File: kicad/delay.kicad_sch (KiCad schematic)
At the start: 58 parts, among them Q1 2N3904, U3 TL074, U4 TL072, U5 PT2399, U6 4020

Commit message: component positioning mostly done
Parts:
- C10, C11, C12, C16, C17, C19, C29, C30, C8: footprint rumblesan-standard-parts:C_Rect_L7.0mm_W3.5mm_P5.00mm -> rumblesan-standard-parts:C_Rect_L7.0mm_W2.5mm_P5.00mm
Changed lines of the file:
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@@
       (effects (font (size 1.27 1.27)) (justify left))
     )
-    (property "Footprint" "rumblesan-standard-parts:C_Rect_L7.0mm_W3.5mm_P5.00mm" (id 2) (at 114.935 232.41 90)
+    (property "Footprint" "rumblesan-standard-parts:C_Rect_L7.0mm_W2.5mm_P5.00mm" (id 2) (at 114.935 232.41 90)
       (effects (font (size 1.27 1.27)) hide)
     )
@@
       (effects (font (size 1.27 1.27)) (justify left))
     )
-    (property "Footprint" "rumblesan-standard-parts:C_Rect_L7.0mm_W3.5mm_P5.00mm" (id 2) (at 114.935 219.71 90)
+    (property "Footprint" "rumblesan-standard-parts:C_Rect_L7.0mm_W2.5mm_P5.00mm" (id 2) (at 114.935 219.71 90)
       (effects (font (size 1.27 1.27)) hide)
     )
@@
       (effects (font (size 1.27 1.27)) (justify left))
     )
-    (property "Footprint" "rumblesan-standard-parts:C_Rect_L7.0mm_W3.5mm_P5.00mm" (id 2) (at 86.995 232.41 90)
+    (property "Footprint" "rumblesan-standard-parts:C_Rect_L7.0mm_W2.5mm_P5.00mm" (id 2) (at 86.995 232.41 90)
       (effects (font (size 1.27 1.27)) hide)
     )
@@
     (property "Reference" "C29" (id 0) (at 288.29 22.8092 90))
     (property "Value" "10pF" (id 1) (at 288.29 25.1206 90))
-    (property "Footprint" "rumblesan-standard-parts:C_Rect_L7.0mm_W3.5mm_P5.00mm" (id 2) (at 289.56 34.925 0)
+    (property "Footprint" "rumblesan-standard-parts:C_Rect_L7.0mm_W2.5mm_P5.00mm" (id 2) (at 289.56 34.925 0)
       (effects (font (size 1.27 1.27)) hide)
     )
@@
     (property "Reference" "C19" (id 0) (at 121.92 48.2092 90))
     (property "Value" "10pF" (id 1) (at 121.92 50.5206 90))
-    (property "Footprint" "rumblesan-standard-parts:C_Rect_L7.0mm_W3.5mm_P5.00mm" (id 2) (at 123.19 60.325 0)
+    (property "Footprint" "rumblesan-standard-parts:C_Rect_L7.0mm_W2.5mm_P5.00mm" (id 2) (at 123.19 60.325 0)
       (effects (font (size 1.27 1.27)) hide)
     )
@@
     (property "Reference" "C8" (id 0) (at 62.23 24.0792 90))
     (property "Value" "10pF" (id 1) (at 62.23 26.3906 90))
-    (property "Footprint" "rumblesan-standard-parts:C_Rect_L7.0mm_W3.5mm_P5.00mm" (id 2) (at 63.5 36.195 0)
+    (property "Footprint" "rumblesan-standard-parts:C_Rect_L7.0mm_W2.5mm_P5.00mm" (id 2) (at 63.5 36.195 0)
       (effects (font (size 1.27 1.27)) hide)
     )
@@
     (property "Reference" "C30" (id 0) (at 340.36 43.1292 90))
     (property "Value" "10pF" (id 1) (at 340.36 45.4406 90))
-    (property "Footprint" "rumblesan-standard-parts:C_Rect_L7.0mm_W3.5mm_P5.00mm" (id 2) (at 341.63 55.245 0)
+    (property "Footprint" "rumblesan-standard-parts:C_Rect_L7.0mm_W2.5mm_P5.00mm" (id 2) (at 341.63 55.245 0)
       (effects (font (size 1.27 1.27)) hide)
     )
@@
       (effects (font (size 1.27 1.27)) (justify left))
     )
-    (property "Footprint" "rumblesan-standard-parts:C_Rect_L7.0mm_W3.5mm_P5.00mm" (id 2) (at 86.995 219.71 90)
+    (property "Footprint" "rumblesan-standard-parts:C_Rect_L7.0mm_W2.5mm_P5.00mm" (id 2) (at 86.995 219.71 90)
       (effects (font (size 1.27 1.27)) hide)
     )
@@
       (effects (font (size 1.27 1.27)) (justify right))
     )
-    (property "Footprint" "rumblesan-standard-parts:C_Rect_L7.0mm_W3.5mm_P5.00mm" (id 2) (at 70.485 140.97 0)
-      (effects (font (size 1.27 1.27)) hide)
-    )
+    (property "Footprint" "rumblesan-standard-parts:C_Rect_L7.0mm_W2.5mm_P5.00mm" (id 2) (at 70.485 140.97 0)
+      (effects (font (size 1.27 1.27)) hide)
+    )

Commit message: initial layout done
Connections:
- net DRY_AUDIO_SOURCE: now also U3.14; no longer U3.7
- net FEEDBACK_SOURCE: now also U3.1; no longer U3.8
- net at C8.2, D5.2 (A), D6.1 (K)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: now also U3.13 (-); no longer U3.6 (-)
- net at C19.1, C22.1, R15.2: now also U3.8; no longer U3.1
- net at C19.2, R13.2, R14.2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: now also U3.9 (-); no longer U3.2 (-)
- net at C29.2, D10.2 (A), D11.1 (K)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: now also U3.2 (-); no longer U3.9 (-)
- net at C30.1, R29.2, R30.1: now also U3.7; no longer U3.14
- net at C30.2, R27.2, R28.1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: now also U3.6 (-); no longer U3.13 (-)
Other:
- moved on the sheet: U3A, U3B, U3C, U3D
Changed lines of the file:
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@@
     (pin "2")
   )
-  (symbol (lib_id "Amplifier_Operational:TL074") (at 62.23 76.2 0) (mirror x) (unit 2)
-    (in_bom yes) (on_board yes) (fields_autoplaced)
-    (property "Reference" "U3" (id 0) (at 62.23 67.4202 0))
-    (property "Value" "TL074" (id 1) (at 62.23 69.9571 0))
-    (property "Footprint" "rumblesan-standard-parts:DIP-14_W7.62mm_Socket" (id 2) (at 60.96 78.74 0)
-      (effects (font (size 1.27 1.27)) hide)
-    )
-    (property "Datasheet" "http://www.ti.com/lit/ds/symlink/tl071.pdf" (id 3) (at 63.5 81.28 0)
+  (symbol (lib_id "Amplifier_Operational:TL074") (at 340.36 74.93 0) (mirror x) (unit 2)
+    (in_bom yes) (on_board yes) (fields_autoplaced)
+    (property "Reference" "U3" (id 0) (at 340.36 66.1502 0))
+    (property "Value" "TL074" (id 1) (at 340.36 68.6871 0))
+    (property "Footprint" "rumblesan-standard-parts:DIP-14_W7.62mm_Socket" (id 2) (at 339.09 77.47 0)
+      (effects (font (size 1.27 1.27)) hide)
+    )
+    (property "Datasheet" "http://www.ti.com/lit/ds/symlink/tl071.pdf" (id 3) (at 341.63 80.01 0)
       (effects (font (size 1.27 1.27)) hide)
     )
@@
     (pin "2")
   )
-  (symbol (lib_id "Amplifier_Operational:TL074") (at 121.92 78.74 0) (mirror x) (unit 1)
-    (in_bom yes) (on_board yes) (fields_autoplaced)
-    (property "Reference" "U3" (id 0) (at 121.92 69.9602 0))
-    (property "Value" "TL074" (id 1) (at 121.92 72.4971 0))
-    (property "Footprint" "rumblesan-standard-parts:DIP-14_W7.62mm_Socket" (id 2) (at 120.65 81.28 0)
-      (effects (font (size 1.27 1.27)) hide)
-    )
-    (property "Datasheet" "http://www.ti.com/lit/ds/symlink/tl071.pdf" (id 3) (at 123.19 83.82 0)
+  (symbol (lib_id "Amplifier_Operational:TL074") (at 288.29 72.39 0) (mirror x) (unit 1)
+    (in_bom yes) (on_board yes) (fields_autoplaced)
+    (property "Reference" "U3" (id 0) (at 288.29 63.6102 0))
+    (property "Value" "TL074" (id 1) (at 288.29 66.1471 0))
+    (property "Footprint" "rumblesan-standard-parts:DIP-14_W7.62mm_Socket" (id 2) (at 287.02 74.93 0)
+      (effects (font (size 1.27 1.27)) hide)
+    )
+    (property "Datasheet" "http://www.ti.com/lit/ds/symlink/tl071.pdf" (id 3) (at 289.56 77.47 0)
       (effects (font (size 1.27 1.27)) hide)
     )
@@
     (pin "2")
   )
-  (symbol (lib_id "Amplifier_Operational:TL074") (at 340.36 74.93 0) (mirror x) (unit 4)
-    (in_bom yes) (on_board yes) (fields_autoplaced)
-    (property "Reference" "U3" (id 0) (at 340.36 66.1502 0))
-    (property "Value" "TL074" (id 1) (at 340.36 68.6871 0))
-    (property "Footprint" "rumblesan-standard-parts:DIP-14_W7.62mm_Socket" (id 2) (at 339.09 77.47 0)
-      (effects (font (size 1.27 1.27)) hide)
-    )
-    (property "Datasheet" "http://www.ti.com/lit/ds/symlink/tl071.pdf" (id 3) (at 341.63 80.01 0)
+  (symbol (lib_id "Amplifier_Operational:TL074") (at 62.23 76.2 0) (mirror x) (unit 4)
+    (in_bom yes) (on_board yes) (fields_autoplaced)
+    (property "Reference" "U3" (id 0) (at 62.23 67.4202 0))
+    (property "Value" "TL074" (id 1) (at 62.23 69.9571 0))
+    (property "Footprint" "rumblesan-standard-parts:DIP-14_W7.62mm_Socket" (id 2) (at 60.96 78.74 0)
+      (effects (font (size 1.27 1.27)) hide)
+    )
+    (property "Datasheet" "http://www.ti.com/lit/ds/symlink/tl071.pdf" (id 3) (at 63.5 81.28 0)
       (effects (font (size 1.27 1.27)) hide)
     )
@@
     (pin "2")
   )
-  (symbol (lib_id "Amplifier_Operational:TL074") (at 288.29 72.39 0) (mirror x) (unit 3)
-    (in_bom yes) (on_board yes) (fields_autoplaced)
-    (property "Reference" "U3" (id 0) (at 288.29 63.6102 0))
-    (property "Value" "TL074" (id 1) (at 288.29 66.1471 0))
-    (property "Footprint" "rumblesan-standard-parts:DIP-14_W7.62mm_Socket" (id 2) (at 287.02 74.93 0)
-      (effects (font (size 1.27 1.27)) hide)
-    )
-    (property "Datasheet" "http://www.ti.com/lit/ds/symlink/tl071.pdf" (id 3) (at 289.56 77.47 0)
-      (effects (font (size 1.27 1.27)) hide)
-    )
+  (symbol (lib_id "Amplifier_Operational:TL074") (at 121.92 78.74 0) (mirror x) (unit 3)
+    (in_bom yes) (on_board yes) (fields_autoplaced)
+    (property "Reference" "U3" (id 0) (at 121.92 69.9602 0))
+    (property "Value" "TL074" (id 1) (at 121.92 72.4971 0))
+    (property "Footprint" "rumblesan-standard-parts:DIP-14_W7.62mm_Socket" (id 2) (at 120.65 81.28 0)
+      (effects (font (size 1.27 1.27)) hide)
+    )
+    (property "Datasheet" "http://www.ti.com/lit/ds/symlink/tl071.pdf" (id 3) (at 123.19 83.82 0)
+      (effects (font (size 1.27 1.27)) hide)
+    )

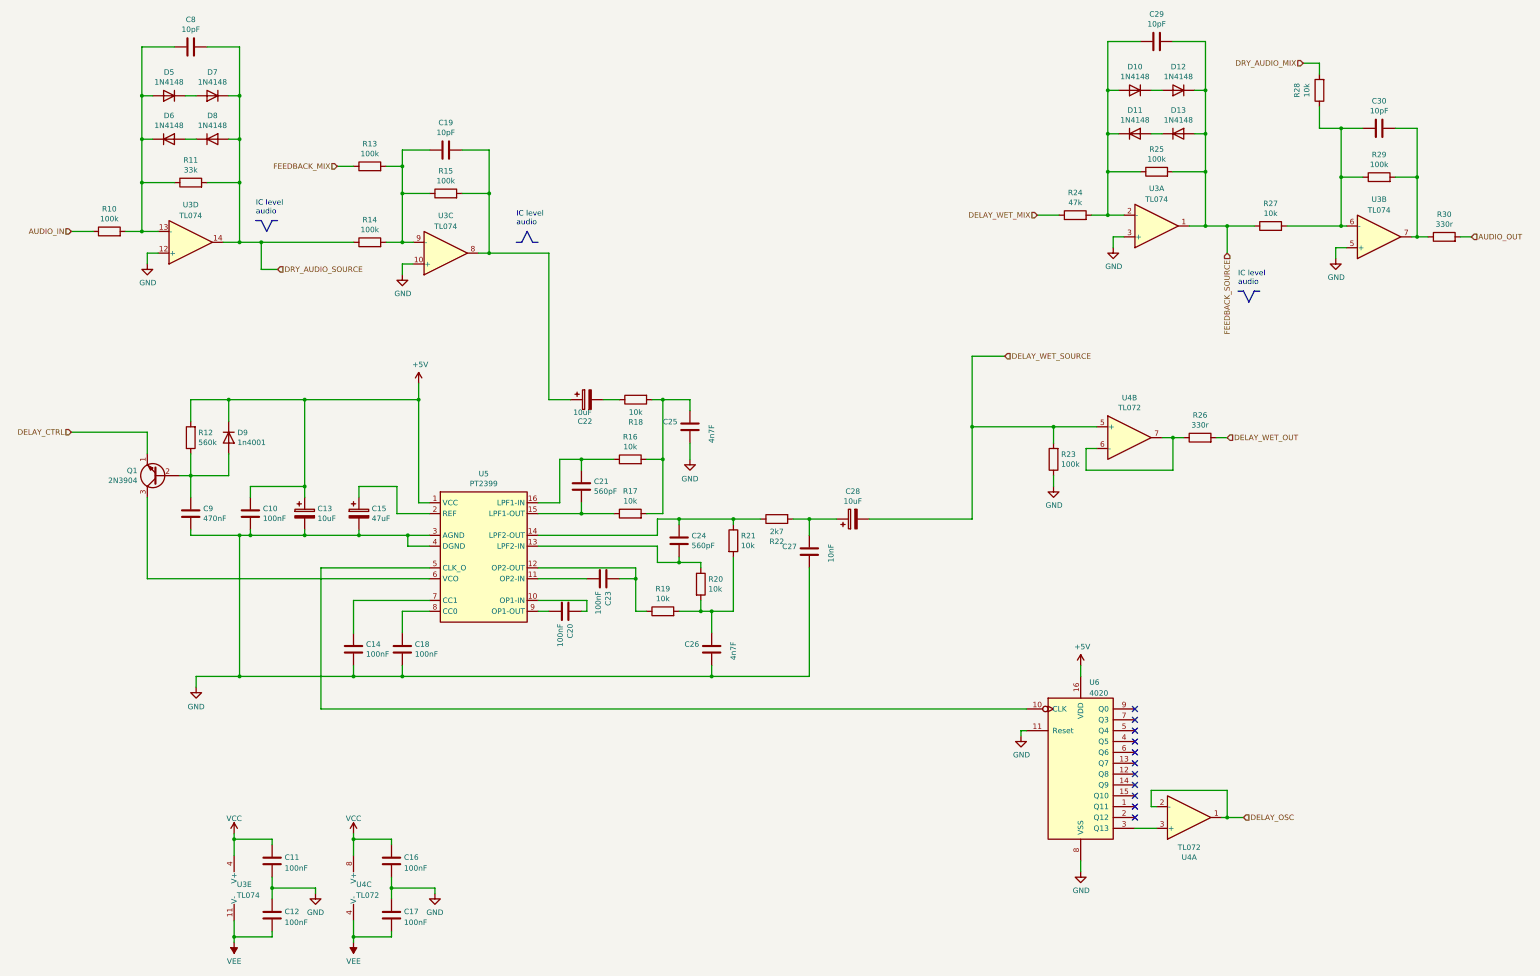
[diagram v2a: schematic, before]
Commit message: Full rejig to use attiny for divider
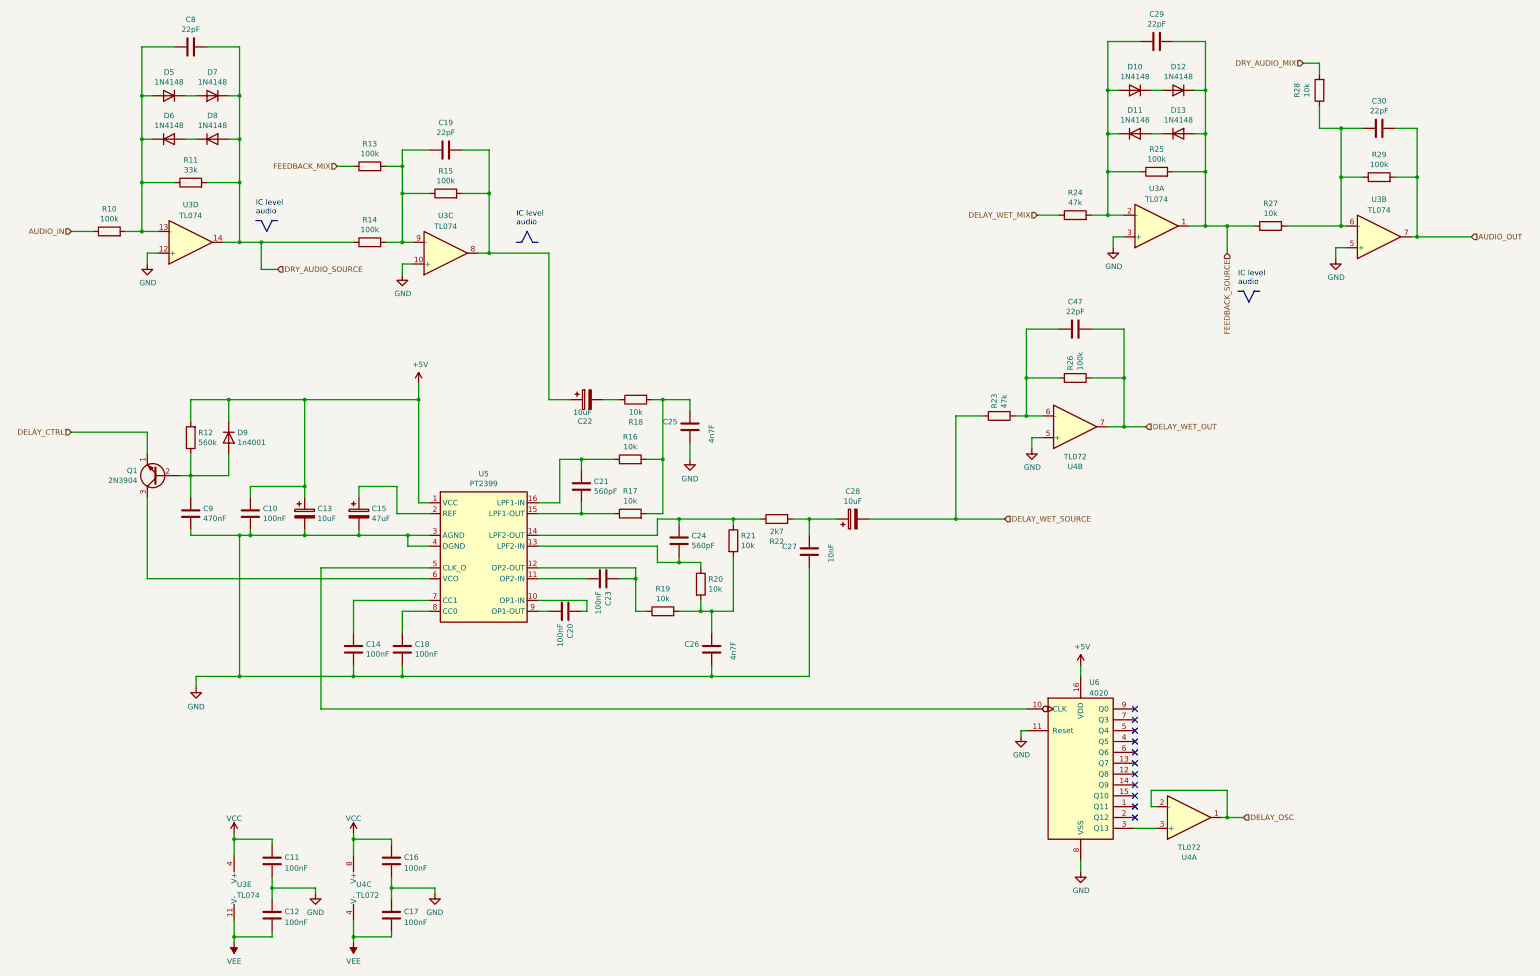
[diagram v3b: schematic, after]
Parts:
- removed R30: 330r, rumblesan-standard-parts:R_Axial_DIN0207_L6.3mm_D2.5mm_P10.16mm_Horizontal, symbol rumblesan-standard-parts:R
- added C47: 22pF, rumblesan-standard-parts:C_Rect_L7.0mm_W2.5mm_P5.00mm, symbol rumblesan-standard-parts:C
- C10, C11, C12, C16, C17, C9: Spec ceramic C0G -> ceramic X7R
- C19, C29, C30, C8: value 10pF -> 22pF
- C27: footprint rumblesan-standard-parts:C_Rect_L7.0mm_W3.5mm_P5.00mm -> rumblesan-standard-parts:C_Rect_L7.0mm_W2.5mm_P5.00mm
- R23: value 100k -> 47k
- R26: value 330r -> 100k
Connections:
- net AUDIO_OUT: now also C30.1, R29.2, U3.7
- net DELAY_WET_OUT: now also R26.1, U4.7, C47.1; no longer R26.2
- net DELAY_WET_SOURCE: no longer U4.5 (+)
- net GND: now also U4.5 (+); no longer R23.1
- new net: C47.2, R23.1, R26.2, U4.6 (-)
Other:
- moved on the sheet: R23, U4B

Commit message: Finished most recent redesign
probably still needs fixing though
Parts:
- C13, C22, C28: footprint rumblesan-standard-parts:CP_Radial_D5.0mm_P2.00mm -> rumblesan-standard-parts:CP_Radial_D5.0mm_L11.0mm_P2.00mm_Horizontal
- C15: footprint rumblesan-standard-parts:CP_Radial_D6.3mm_P2.50mm -> rumblesan-standard-parts:CP_Radial_D6.3.0mm_L11.0mm_P2.00mm_Horizontal
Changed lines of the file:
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@@
       (effects (font (size 1.27 1.27)) (justify left))
     )
-    (property "Footprint" "rumblesan-standard-parts:CP_Radial_D5.0mm_P2.00mm" (id 2) (at 158.75 113.9952 0)
+    (property "Footprint" "rumblesan-standard-parts:CP_Radial_D5.0mm_L11.0mm_P2.00mm_Horizontal" (id 2) (at 158.75 113.9952 0)
       (effects (font (size 1.27 1.27)) hide)
     )
@@
       (effects (font (size 1.27 1.27)) (justify left))
     )
-    (property "Footprint" "rumblesan-standard-parts:CP_Radial_D5.0mm_P2.00mm" (id 2) (at 89.8652 143.51 0)
+    (property "Footprint" "rumblesan-standard-parts:CP_Radial_D5.0mm_L11.0mm_P2.00mm_Horizontal" (id 2) (at 89.8652 143.51 0)
       (effects (font (size 1.27 1.27)) hide)
     )
@@
       (effects (font (size 1.27 1.27)) (justify left))
     )
-    (property "Footprint" "rumblesan-standard-parts:CP_Radial_D6.3mm_P2.50mm" (id 2) (at 102.5652 143.51 0)
+    (property "Footprint" "rumblesan-standard-parts:CP_Radial_D6.3.0mm_L11.0mm_P2.00mm_Horizontal" (id 2) (at 102.5652 143.51 0)
       (effects (font (size 1.27 1.27)) hide)
     )
@@
     (property "Reference" "C28" (id 0) (at 217.17 134.493 90))
     (property "Value" "10uF" (id 1) (at 217.17 136.8044 90))
-    (property "Footprint" "rumblesan-standard-parts:CP_Radial_D5.0mm_P2.00mm" (id 2) (at 220.98 140.0048 0)
-      (effects (font (size 1.27 1.27)) hide)
-    )
+    (property "Footprint" "rumblesan-standard-parts:CP_Radial_D5.0mm_L11.0mm_P2.00mm_Horizontal" (id 2) (at 220.98 140.0048 0)
+      (effects (font (size 1.27 1.27)) hide)
+    )

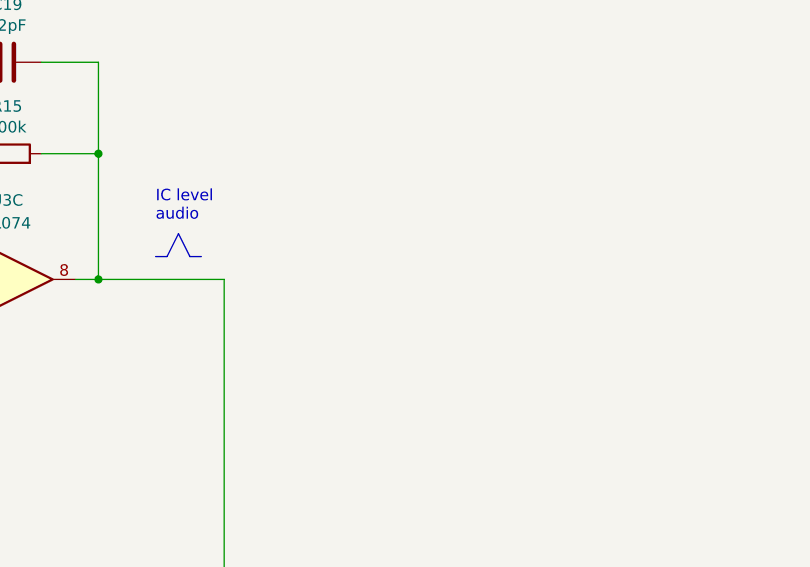
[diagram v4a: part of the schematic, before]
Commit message: Layout seems to be all done, though needs further checking
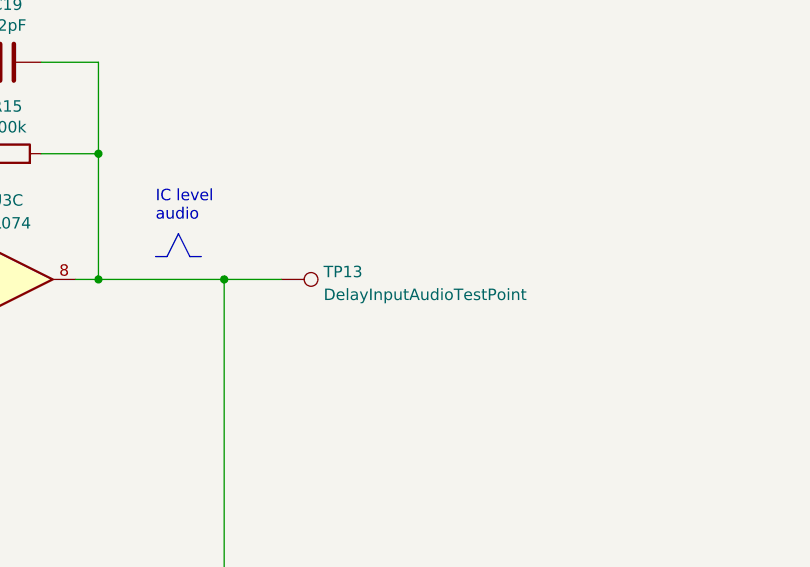
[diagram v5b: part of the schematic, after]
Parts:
- added TP13: DelayInputAudioTestPoint, rumblesan-standard-parts:TestPoint_Loop_D2.50mm_Drill1.0mm_LowProfile, symbol Connector:TestPoint
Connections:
- net at C19.1, C22.1, R15.2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: now also TP13.1
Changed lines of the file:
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@@
   (junction (at 299.72 50.8) (diameter 0) (color 0 0 0 0)
+  )
+  (junction (at 146.05 78.74) (diameter 0) (color 0 0 0 0)
   )
   (junction (at 50.8 41.91) (diameter 0) (color 0 0 0 0)
@@
     (stroke (width 0) (type default) (color 0 0 0 0))
   )
+  (wire (pts (xy 146.05 78.74) (xy 152.4 78.74))
+    (stroke (width 0) (type default) (color 0 0 0 0))
+  )
   (wire (pts (xy 73.66 177.8) (xy 63.5 177.8))
     (stroke (width 0) (type default) (color 0 0 0 0))
@@
     (pin "2")
   )
+  (symbol (lib_id "Connector:TestPoint") (at 152.4 78.74 270) (unit 1)
+    (in_bom yes) (on_board yes) (fields_autoplaced)
+    (property "Reference" "TP13" (id 0) (at 157.099 77.9053 90)
+      (effects (font (size 1.27 1.27)) (justify left))
+    )
+    (property "Value" "DelayInputAudioTestPoint" (id 1) (at 157.099 80.4422 90)
+      (effects (font (size 1.27 1.27)) (justify left))
+    )
+    (property "Footprint" "rumblesan-standard-parts:TestPoint_Loop_D2.50mm_Drill1.0mm_LowProfile" (id 2) (at 152.4 83.82 0)
+      (effects (font (size 1.27 1.27)) hide)
+    )
+    (property "Datasheet" "~" (id 3) (at 152.4 83.82 0)
+      (effects (font (size 1.27 1.27)) hide)
+    )
+    (pin "1")
+  )
   (symbol (lib_id "Amplifier_Operational:TL072") (at 295.91 210.82 0) (mirror x) (unit 1)

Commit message: Changing name to the mercurial machine
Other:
- title: Dual Digi Delay -> The Mercurial Machine
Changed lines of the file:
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@@
   (paper "A3")
   (title_block
-    (title "Dual Digi Delay")
-    (date "2022-03-04")
-    (rev "v05")
+    (title "The Mercurial Machine")
+    (date "2023-05-13")
+    (rev "r02")
     (comment 2 "creativecommons.org/licenses/by/4.0/")
     (comment 3 "License: CC BY 4.0")

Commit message: geographically reannotate parts
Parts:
- renumbered C17 to C11, C16 to C12, C47 to C13, C19 to C14, C12 to C15, C8 to C16, C10 to C17, C9 to C18, C14 to C19, C18 to C20, C28 to C21, C11 to C23, C29 to C24, C30 to C25, C20 to C26, C15 to C27, C21 to C28, C24 to C29, C23 to C30, C13 to C32, C27 to C34, C26 to C36, C25 to C38, D5 to D1, D7 to D2, D6 to D3, D8 to D4, D9 to D5, D12 to D6, D13 to D8, D10 to D9, Q1 to Q3, R23 to R47, R10 to R48, R13 to R49, R11 to R50, R26 to R51, R15 to R52, R14 to R53, R12 to R54, R24 to R56, R28 to R59, R27 to R60, R29 to R62, R25 to R63, R19 to R64, R16 to R67, R17 to R68, R22 to R69, R21 to R70, R20 to R71, R18 to R80, TP13 to TP15, U6 to U3, U3 to U5, U5 to U6

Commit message: Changing name again
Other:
- title: The Mercurial Machine -> Ouroboros
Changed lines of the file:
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@@
   (paper "A3")
   (title_block
-    (title "The Mercurial Machine")
+    (title "Ouroboros")
     (date "2023-05-13")
     (rev "r02")
